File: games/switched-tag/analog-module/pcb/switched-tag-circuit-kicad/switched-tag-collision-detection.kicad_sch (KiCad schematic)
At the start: 25 parts

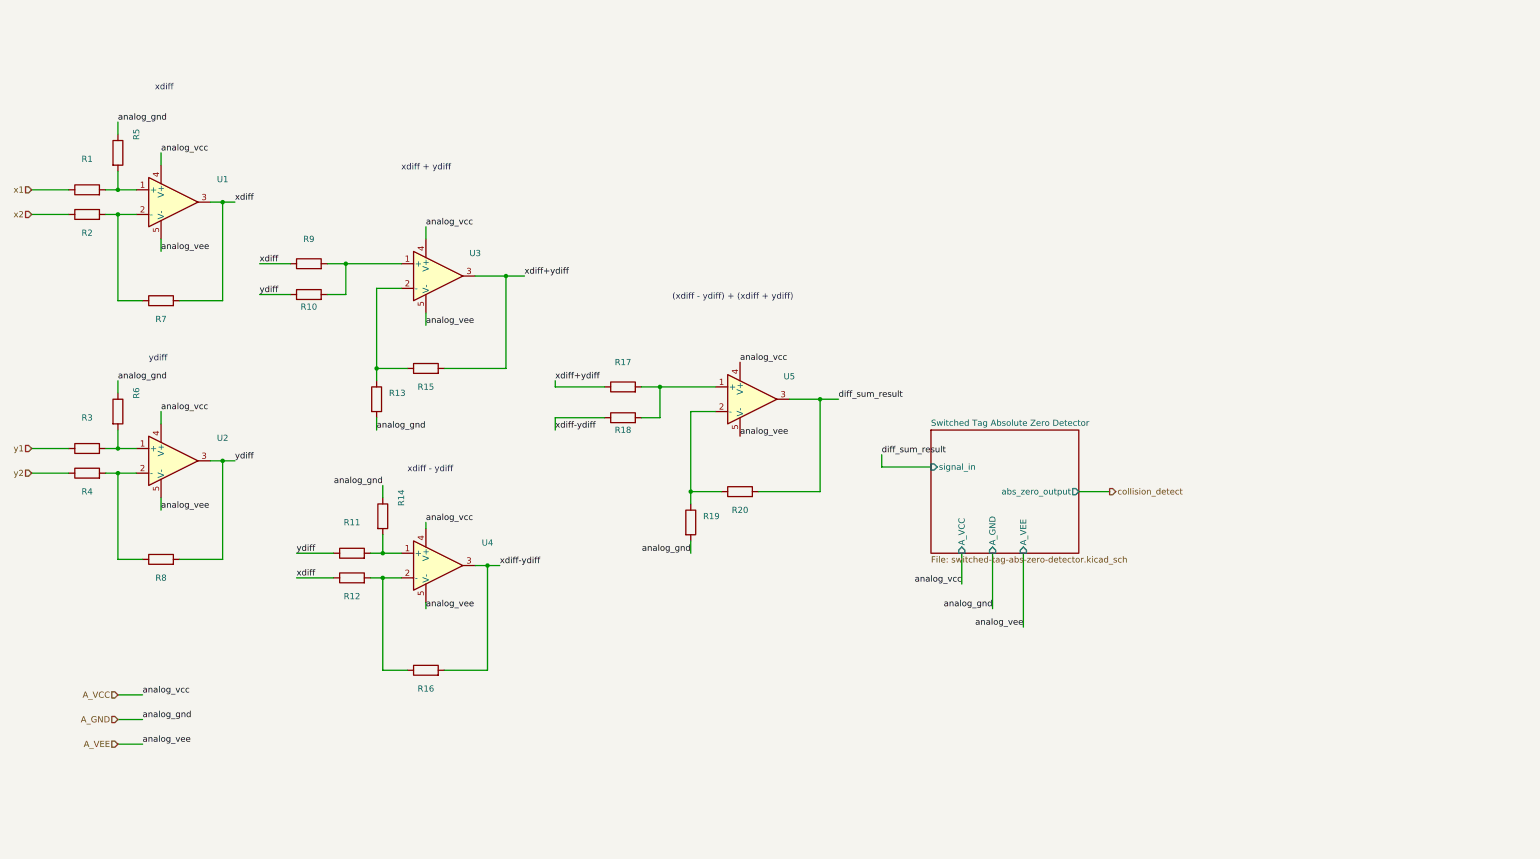
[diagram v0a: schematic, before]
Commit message: Converted Lm358.mod to .lib file for convenience.
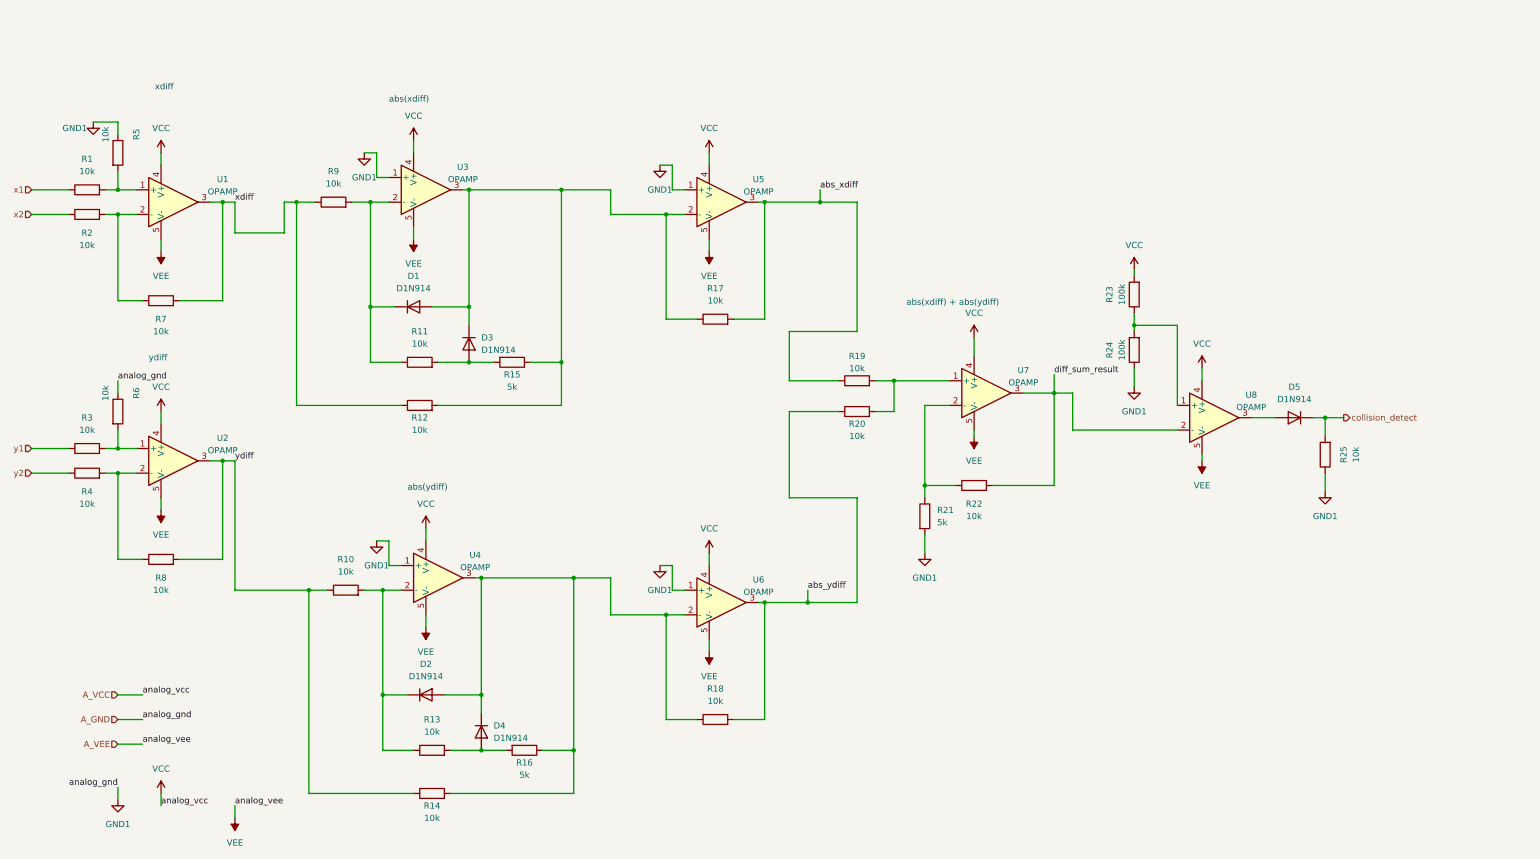
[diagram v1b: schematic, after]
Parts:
- added D1, D2, D3, D4, D5: D1N914, symbol Device:D
- added R17, R18, R25: 10k, symbol Device:R
- added R23, R24: 100k, symbol Device:R
- added U5, U6, U8: OPAMP, symbol Simulation_SPICE:OPAMP
- R1, R10, R11, R12, R13, R14, R2, R3, R4, R5, R6, R7, R8, R9: value (none) -> 10k
- R15, R16: value (none) -> 5k
- R19: renamed from R17; value (none) -> 10k
- R20: renamed from R18; value (none) -> 10k
- R21: renamed from R19; value (none) -> 5k
- R22: renamed from R20; value (none) -> 10k
- U1, U2, U3, U4: value (none) -> OPAMP; Spice_Lib_File /home/pab/Inventions/analog-circuit-game-console/ms-circuit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 -> (none); Spice_Model AD8031 -> (none); Spice_Netlist_Enabled Y -> (none); Spice_Node_Sequence 1 2 4 5 3 -> (none); Spice_Primitive X -> (none)
- U7: renamed from U5; value (none) -> OPAMP; Spice_Lib_File /home/pab/Inventions/analog-circuit-game-console/ms-circuit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 -> (none); Spice_Model AD8031 -> (none); Spice_Netlist_Enabled Y -> (none); Spice_Node_Sequence 1 2 4 5 3 -> (none); Spice_Primitive X -> (none)
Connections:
- net collision_detect: now also D5.1 (K), R25.2
- net diff_sum_result: now also U8.2 (-)
- net ydiff: now also R14.1; no longer R11.1
- net A_GND renamed GND1
- net GND1: now also U3.1 (+), U4.1 (+), R24.1, R25.1, U5.1 (+), U6.1 (+); no longer R13.2, R14.1
- net A_VCC renamed VCC
- net VCC: now also R23.2, U5.4 (V+), U6.4 (V+), U8.4 (V+)
- net A_VEE renamed VEE
- net VEE: now also U5.5 (V-), U6.5 (V-), U8.5 (V-)
- removed net xdiff+ydiff: R15.2, R19.1, U3.3
- removed net xdiff-ydiff: R16.2, R20.1, U4.3
- new net: D1.2 (A), D3.1 (K), R12.2, R15.1, R17.1, U3.3, U5.2 (-)
- new net: D3.2 (A), R11.2, R15.2
- new net: D2.2 (A), D4.1 (K), R14.2, R16.1, R18.1, U4.3, U6.2 (-)
- new net: D1.1 (K), R11.1, R9.2, U3.2 (-)
- new net: D2.1 (K), R10.2, R13.1, U4.2 (-)
- new net: D4.2 (A), R13.2, R16.2
- new net: R23.1, R24.2, U8.1 (+)
- new net: D5.2 (A), U8.3
- new net abs_xdiff: R17.2, R19.1, U5.3
- new net abs_ydiff: R18.2, R20.1, U6.3
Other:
- removed sheet Switched Tag Absolute Zero Detector
- note added: "abs(xdiff)"
- note added: "abs(xdiff) + abs(ydiff)"
- note added: "abs(ydiff)"
- note removed: "(xdiff - ydiff) + (xdiff + ydiff)"
- note removed: "xdiff + ydiff"
- note removed: "xdiff - ydiff"
- moved on the sheet: R19, R20, R21, R22, U3, U7

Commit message: Updated simulation schematic. Need to fix timestep too small problem.
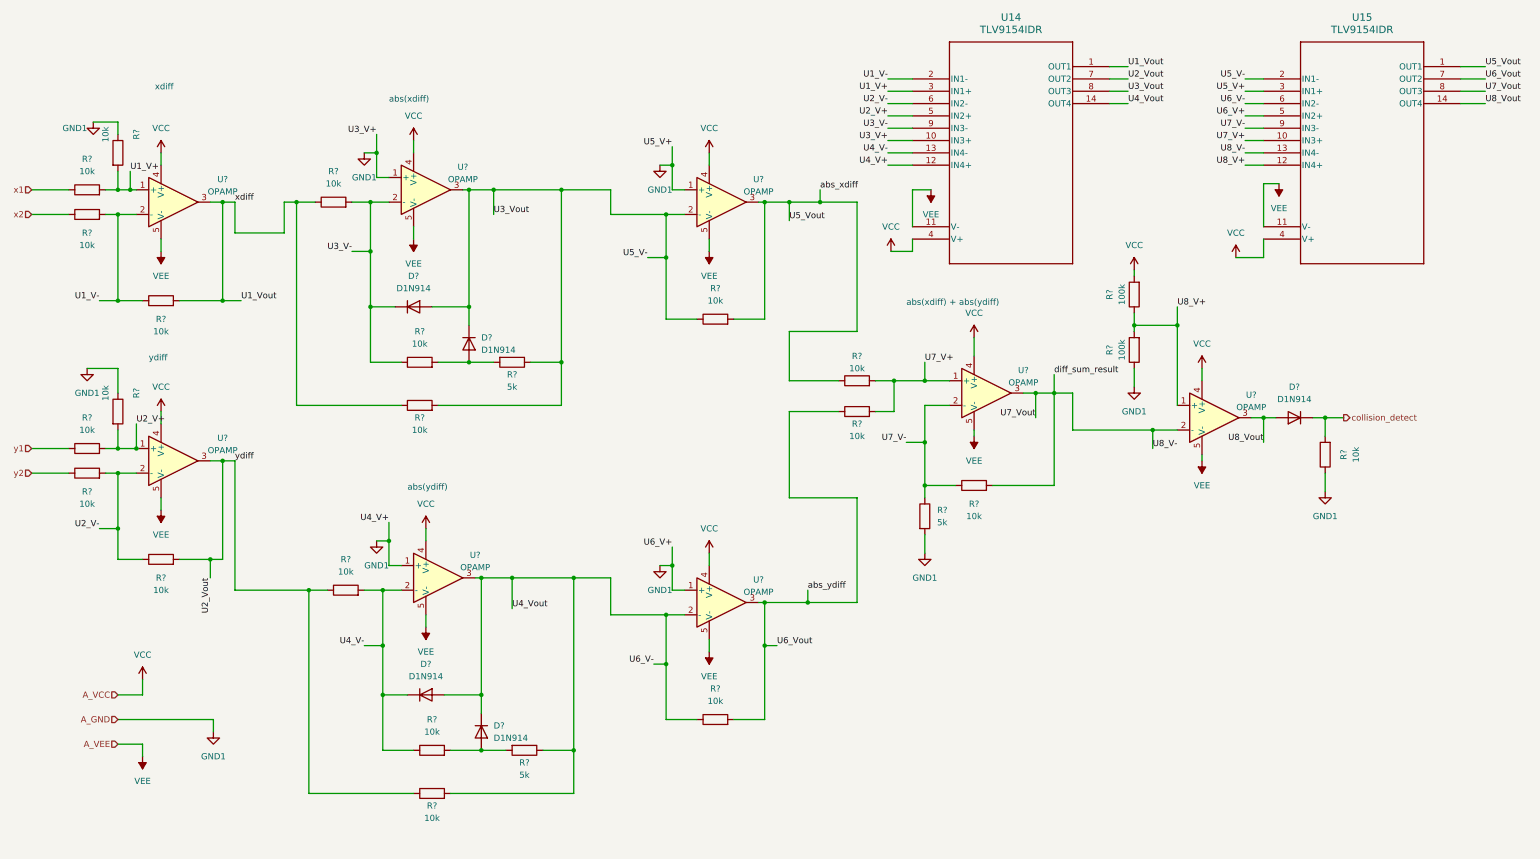
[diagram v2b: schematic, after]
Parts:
- added U14, U15: TLV9154IDR, SOIC_9154IDR_TEX, symbol switched-tag-symbol-lib:TLV9154IDR
- U?: renamed from U5; now left out of the parts list
- U?: renamed from U7; now left out of the parts list
- U?: renamed from U3; now left out of the parts list
- U?: renamed from U4; now left out of the parts list
- U?: renamed from U2; now left out of the parts list
- U?: renamed from U1; now left out of the parts list
- U?: renamed from U8; now left out of the parts list
- U?: renamed from U6; now left out of the parts list
- renumbered D3 to D?, D4 to D?, D5 to D?, D2 to D?, D1 to D?, R22 to R?, R15 to R?, R14 to R?, R20 to R?, R7 to R?, R8 to R?, R12 to R?, R16 to R?, R11 to R?, R24 to R?, R18 to R?, R17 to R?, R6 to R?, R9 to R?, R1 to R?, R2 to R?, R10 to R?, R13 to R?, R25 to R?, R19 to R?, R5 to R?, R4 to R?, R3 to R?, R21 to R?, R23 to R?
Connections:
- net GND1: now also U14.10 (IN3+), U14.12 (IN4+), U15.3 (IN1+), U15.5 (IN2+)
- net VCC: now also U14.4 (V+), U15.4 (V+)
- net VEE: now also U14.11 (V-), U15.11 (V-)
- net U7_V-: now reaches R?.1, R?.1, U?.2 (-)
- net U7_V-: now also U15.9 (IN3-)
- net U3_Vout: now reaches D?.1 (K), D?.2 (A), R?.1, R?.1, R?.2, U?.2 (-), U?.3
- net U3_Vout: now also U14.8 (OUT3), U15.2 (IN1-)
- net U4_Vout: now reaches D?.1 (K), D?.2 (A), R?.1, R?.1, R?.2, U?.2 (-), U?.3
- net U4_Vout: now also U14.14 (OUT4), U15.6 (IN2-)
- net U7_V+: now reaches R?.2, R?.2, U?.1 (+)
- net U7_V+: now also U15.10 (IN3+)
- net U3_V-: now reaches D?.1 (K), R?.1, R?.2, U?.2 (-)
- net U3_V-: now also U14.9 (IN3-)
- net U4_V-: now reaches D?.1 (K), R?.1, R?.2, U?.2 (-)
- net U4_V-: now also U14.13 (IN4-)
- net U2_V+: now reaches R?.2, R?.2, U?.1 (+)
- net U2_V+: now also U14.5 (IN2+)
- net U2_V-: now reaches R?.1, R?.2, U?.2 (-)
- net U2_V-: now also U14.6 (IN2-)
- net U1_V-: now reaches R?.1, R?.2, U?.2 (-)
- net U1_V-: now also U14.2 (IN1-)
- net U8_V+: now reaches R?.1, R?.2, U?.1 (+)
- net U8_V+: now also U15.12 (IN4+)
- net U1_V+: now reaches R?.2, R?.2, U?.1 (+)
- net U1_V+: now also U14.3 (IN1+)
- net U8_Vout: now reaches D?.2 (A), U?.3
- net U8_Vout: now also U15.14 (OUT4)
- net abs_xdiff renamed U5_Vout
- net U5_Vout: now also U15.1 (OUT1)
- net abs_ydiff renamed U6_Vout
- net U6_Vout: now also U15.7 (OUT2)
- net diff_sum_result renamed U7_Vout
- net U7_Vout: now also U15.13 (IN4-), U15.8 (OUT3)
- net xdiff renamed U1_Vout
- net U1_Vout: now also U14.1 (OUT1)
- net ydiff renamed U2_Vout
- net U2_Vout: now also U14.7 (OUT2)

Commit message: Started pcb with placeholder components. Incomplete PCB.
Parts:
- D? (x5): footprint (none) -> Diode_SMD:D_0603_1608Metric
- R? (x25): footprint (none) -> Resistor_SMD:R_0603_1608Metric
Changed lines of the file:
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@@
       (effects (font (size 1.27 1.27)))
     )
-    (property "Footprint" "" (at 214.63 110.998 90)
+    (property "Footprint" "Resistor_SMD:R_0603_1608Metric" (at 214.63 110.998 90)
       (effects (font (size 1.27 1.27)) hide)
     )
@@
       (effects (font (size 1.27 1.27)))
     )
-    (property "Footprint" "" (at 119.38 82.042 90)
+    (property "Footprint" "Resistor_SMD:R_0603_1608Metric" (at 119.38 82.042 90)
       (effects (font (size 1.27 1.27)) hide)
     )
@@
       (effects (font (size 1.27 1.27)))
     )
-    (property "Footprint" "" (at 102.87 174.498 90)
+    (property "Footprint" "Resistor_SMD:R_0603_1608Metric" (at 102.87 174.498 90)
       (effects (font (size 1.27 1.27)) hide)
     )
@@
       (effects (font (size 1.27 1.27)))
     )
-    (property "Footprint" "" (at 190.5 95.758 90)
+    (property "Footprint" "Resistor_SMD:R_0603_1608Metric" (at 190.5 95.758 90)
       (effects (font (size 1.27 1.27)) hide)
     )
@@
       (effects (font (size 1.27 1.27)))
     )
-    (property "Footprint" "" (at 46.99 72.898 90)
+    (property "Footprint" "Resistor_SMD:R_0603_1608Metric" (at 46.99 72.898 90)
       (effects (font (size 1.27 1.27)) hide)
     )
@@
       (effects (font (size 1.27 1.27)))
     )
-    (property "Footprint" "" (at 46.99 126.238 90)
+    (property "Footprint" "Resistor_SMD:R_0603_1608Metric" (at 46.99 126.238 90)
       (effects (font (size 1.27 1.27)) hide)
     )
@@
       (effects (font (size 1.27 1.27)))
     )
-    (property "Footprint" "" (at 100.33 94.488 90)
+    (property "Footprint" "Resistor_SMD:R_0603_1608Metric" (at 100.33 94.488 90)
       (effects (font (size 1.27 1.27)) hide)
     )
@@
       (effects (font (size 1.27 1.27)))
     )
-    (property "Footprint" "" (at 121.92 162.052 90)
+    (property "Footprint" "Resistor_SMD:R_0603_1608Metric" (at 121.92 162.052 90)
       (effects (font (size 1.27 1.27)) hide)
     )
@@
       (effects (font (size 1.27 1.27)))
     )
-    (property "Footprint" "" (at 100.33 85.598 90)
+    (property "Footprint" "Resistor_SMD:R_0603_1608Metric" (at 100.33 85.598 90)
       (effects (font (size 1.27 1.27)) hide)
     )
@@
       (effects (font (size 1.27 1.27)))
     )
-    (property "Footprint" "" (at 249.428 81.28 90)
+    (property "Footprint" "Resistor_SMD:R_0603_1608Metric" (at 249.428 81.28 90)
       (effects (font (size 1.27 1.27)) hide)
     )
@@
       (effects (font (size 1.27 1.27)))
     )
-    (property "Footprint" "" (at 161.29 159.258 90)
+    (property "Footprint" "Resistor_SMD:R_0603_1608Metric" (at 161.29 159.258 90)
       (effects (font (size 1.27 1.27)) hide)
     )
@@
       (effects (font (size 1.27 1.27)) (justify left))
     )
-    (property "Footprint" "" (at 110.49 80.01 0)
+    (property "Footprint" "Diode_SMD:D_0603_1608Metric" (at 110.49 80.01 0)
       (effects (font (size 1.27 1.27)) hide)
     )
@@
       (effects (font (size 1.27 1.27)))
     )
-    (property "Footprint" "" (at 161.29 76.708 90)
+    (property "Footprint" "Resistor_SMD:R_0603_1608Metric" (at 161.29 76.708 90)
       (effects (font (size 1.27 1.27)) hide)
     )
@@
       (effects (font (size 1.27 1.27)))
     )
-    (property "Footprint" "" (at 36.322 93.98 90)
+    (property "Footprint" "Resistor_SMD:R_0603_1608Metric" (at 36.322 93.98 90)
       (effects (font (size 1.27 1.27)) hide)
     )
@@
       (effects (font (size 1.27 1.27)))
     )
-    (property "Footprint" "" (at 82.55 52.578 90)
+    (property "Footprint" "Resistor_SMD:R_0603_1608Metric" (at 82.55 52.578 90)
       (effects (font (size 1.27 1.27)) hide)
     )
@@
       (effects (font (size 1.27 1.27)))
     )
-    (property "Footprint" "" (at 31.75 50.038 90)
+    (property "Footprint" "Resistor_SMD:R_0603_1608Metric" (at 31.75 50.038 90)
       (effects (font (size 1.27 1.27)) hide)
     )
@@
       (effects (font (size 1.27 1.27)))
     )
-    (property "Footprint" "" (at 31.75 55.118 90)
+    (property "Footprint" "Resistor_SMD:R_0603_1608Metric" (at 31.75 55.118 90)
       (effects (font (size 1.27 1.27)) hide)
     )
@@
       (effects (font (size 1.27 1.27)))
     )
-    (property "Footprint" "" (at 85.09 132.588 90)
+    (property "Footprint" "Resistor_SMD:R_0603_1608Metric" (at 85.09 132.588 90)
       (effects (font (size 1.27 1.27)) hide)
     )
@@
       (effects (font (size 1.27 1.27)) (justify left))
     )
-    (property "Footprint" "" (at 113.03 160.02 0)
+    (property "Footprint" "Diode_SMD:D_0603_1608Metric" (at 113.03 160.02 0)
       (effects (font (size 1.27 1.27)) hide)
     )
@@
       (effects (font (size 1.27 1.27)))
     )
-    (property "Footprint" "" (at 102.87 165.608 90)
+    (property "Footprint" "Resistor_SMD:R_0603_1608Metric" (at 102.87 165.608 90)
       (effects (font (size 1.27 1.27)) hide)
     )
@@
       (effects (font (size 1.27 1.27)))
     )
-    (property "Footprint" "" (at 288.798 102.87 90)
+    (property "Footprint" "Resistor_SMD:R_0603_1608Metric" (at 288.798 102.87 90)
       (effects (font (size 1.27 1.27)) hide)
     )
@@
       (effects (font (size 1.27 1.27)))
     )
-    (property "Footprint" "" (at 190.5 89.408 90)
+    (property "Footprint" "Resistor_SMD:R_0603_1608Metric" (at 190.5 89.408 90)
       (effects (font (size 1.27 1.27)) hide)
     )
@@
       (effects (font (size 1.27 1.27)))
     )
-    (property "Footprint" "" (at 36.322 40.64 90)
+    (property "Footprint" "Resistor_SMD:R_0603_1608Metric" (at 36.322 40.64 90)
       (effects (font (size 1.27 1.27)) hide)
     )
@@
       (effects (font (size 1.27 1.27)))
     )
-    (property "Footprint" "" (at 31.75 108.458 90)
+    (property "Footprint" "Resistor_SMD:R_0603_1608Metric" (at 31.75 108.458 90)
       (effects (font (size 1.27 1.27)) hide)
     )
@@
       (effects (font (size 1.27 1.27)))
     )
-    (property "Footprint" "" (at 280.67 95.25 0)
+    (property "Footprint" "Diode_SMD:D_0603_1608Metric" (at 280.67 95.25 0)
       (effects (font (size 1.27 1.27)) hide)
     )
@@
       (effects (font (size 1.27 1.27)))
     )
-    (property "Footprint" "" (at 31.75 103.378 90)
+    (property "Footprint" "Resistor_SMD:R_0603_1608Metric" (at 31.75 103.378 90)
       (effects (font (size 1.27 1.27)) hide)
     )
@@
       (effects (font (size 1.27 1.27)))
     )
-    (property "Footprint" "" (at 101.6 152.4 0)
+    (property "Footprint" "Diode_SMD:D_0603_1608Metric" (at 101.6 152.4 0)
       (effects (font (size 1.27 1.27)) hide)
     )
@@
       (effects (font (size 1.27 1.27)) (justify left))
     )
-    (property "Footprint" "" (at 202.692 115.57 90)
+    (property "Footprint" "Resistor_SMD:R_0603_1608Metric" (at 202.692 115.57 90)
       (effects (font (size 1.27 1.27)) hide)
     )
@@
       (effects (font (size 1.27 1.27)))
     )
-    (property "Footprint" "" (at 249.428 69.85 90)
+    (property "Footprint" "Resistor_SMD:R_0603_1608Metric" (at 249.428 69.85 90)
       (effects (font (size 1.27 1.27)) hide)
     )
@@
       (effects (font (size 1.27 1.27)))
     )
-    (property "Footprint" "" (at 99.06 72.39 0)
-      (effects (font (size 1.27 1.27)) hide)
-    )
+    (property "Footprint" "Diode_SMD:D_0603_1608Metric" (at 99.06 72.39 0)
+      (effects (font (size 1.27 1.27)) hide)
+    )
